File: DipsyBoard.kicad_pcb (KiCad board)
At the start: 2 copper layers, 30.5 x 45.7 mm, 28 parts, among them P2 CONN_01X16, P3 CONN_01X16, U1 STM32L486Rx-LQFP64, U2 LD1117S50TR, U4 PUSBMxX4, U5 TPS56x200, Y1 16MHz

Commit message: Last changes
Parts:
- removed C10, C11: 22pF, Capacitors_SMD:C_0603
- removed C15: 0.1u, Capacitors_SMD:C_0603
- removed C16: 22uF, Capacitors_SMD:C_1206
- removed L1: 3.3uH, SMD_Packages:SMD-1210_Pol
- removed R1: 33.2k, Resistors_SMD:R_0603
- removed R2: 10.0k, Resistors_SMD:R_0603
- removed U5: TPS56x200, Housings_SOT-23_SOT-143_TSOT-6:SOT-23-6
- removed Y1: 16MHz, Crystals:Crystal_SMD_0603_4Pads
- added C18: 0.1uF, w_smd_cap:c_0603, F.Cu at (151.2, 119.7)
- added CON1: SD_Card, xess:xess-SCHD3A0100, B.Cu at (144.7, 129.1)
- added P1: USB_OTG, w_conn_pc:conn_usb_B_mini_smd, F.Cu at (144.8, 100.3)
- added P6: JTAG, engstad:conn-jtag-0.05, B.Cu at (144.8, 101.7)
- added SW1: RESET, Buttons_Switches_SMD:SW_SPST_EVPBF, F.Cu at (145.0, 142.7)
- added U3: NCP1117DT33G, w_smd_trans:sot223, F.Cu at (149.6, 113.0)
- added X1: XTAL, engstad:cstce-v-c, F.Cu at (140.6, 119.5)
- C1, C5, C6, C7, C8, C9: footprint Capacitors_SMD:C_0603 -> w_smd_cap:c_0603
- C12, C13, C14, C2, C3, C4: footprint Capacitors_SMD:C_0805 -> w_smd_cap:c_0805
- C17: footprint Capacitors_SMD:C_1206 -> w_smd_cap:c_1206
- P2, P3: value CONN_01X16 -> CONN_01X19; footprint Pin_Headers:Pin_Header_Straight_1x16 -> w_pin_strip:pin_strip_19
- U2: value LD1117S50TR -> NCP1117ST50T3G; footprint Housings_SOT-23_SOT-143_TSOT-6:SOT-23 -> w_smd_trans:sot223
- moved C1 82.8 mm to (139.2, 142.7), turned to 90 degrees
- moved C7 76.9 mm to (150.2, 136.4), turned to 90 degrees
- moved C6 72.3 mm to (137.0, 122.4), turned to 270 degrees
- moved C2 63.1 mm to (140.8, 135.8)
- moved C9 62.6 mm to (140.5, 137.6)
- moved C8 50.3 mm to (149.5, 119.7), turned to 270 degrees
- moved C5 49.5 mm to (147.8, 119.7), turned to 270 degrees
- moved C3 47.2 mm to (137.2, 125.8), turned to 90 degrees
- moved C4 45.9 mm to (152.3, 134.9), turned to 90 degrees
- moved C13 44.5 mm to (152.0, 100.5), turned to 90 degrees
- moved C12 41.8 mm to (140.9, 107.3), turned to 180 degrees
- moved C14 36.1 mm to (149.9, 107.3), turned to 180 degrees
- moved D1 34.6 mm to (145.4, 107.3), turned to 180 degrees
- moved U4 31.2 mm to (145.1, 117.0)
- moved U2 30.2 mm to (139.9, 113.0), turned to 180 degrees
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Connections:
- net /OTG_FS_DM renamed /OTG_FS_D-
- net /OTG_FS_DP renamed /OTG_FS_D+
- C13 pad 1: Net-(C13-Pad1) -> /+5V
- D1 pad 2: Net-(C13-Pad1) -> /+5V
- P2 pad 1: /D1 -> /+5V
- P2 pad 11: /D11 -> /D9
- P2 pad 12: /D12 -> /D8
- P2 pad 13: /D13 -> /D7
- P2 pad 14: /D14 -> /D6
- P2 pad 15: /D15 -> /D5
- P2 pad 16: /D16 -> /D4
- P2 pad 2: /D2 -> GND
- P2 pad 3: /D3 -> /VDD
- P2 pad 4: /D4 -> /D16
- P2 pad 5: /D5 -> /D15
- P2 pad 6: /D6 -> /D14
- P2 pad 7: /D7 -> /D13
- P2 pad 8: /D8 -> /D12
- P2 pad 9: /D9 -> /D11
- P3 pad 1: /A1 -> /VIN
- P3 pad 10: /A10 -> /A7
- P3 pad 11: /A11 -> /A8
- P3 pad 12: /A12 -> /A9
- P3 pad 13: /A13 -> /A10
- P3 pad 14: /A14 -> /A11
- P3 pad 15: /A15 -> /A12
- P3 pad 16: /A16 -> /A13
- P3 pad 2: /A2 -> GND
- P3 pad 3: /A3 -> /RTC_OUT
- P3 pad 4: /A4 -> /A1
- P3 pad 5: /A5 -> /A2
- P3 pad 6: /A6 -> /A3
- P3 pad 7: /A7 -> /A4
- P3 pad 8: /A8 -> /A5
- P3 pad 9: /A9 -> /A6
- U1 pad 29: /D7 -> /D2
- U1 pad 30: /D8 -> /D3
- U1 pad 33: /D9 -> /D4
- U1 pad 34: /D10 -> /D5
- U1 pad 35: /D11 -> /D6
- U1 pad 36: /D12 -> /D7
- U1 pad 37: /D14 -> /D8
- U1 pad 38: /D15 -> /D9
- U1 pad 41: /OTG_FS_SOF -> /D10
- U1 pad 42: /OTG_FS_VBUS -> /D11
- U1 pad 57: /D2 -> /D12
- U1 pad 58: /D3 -> /D13
- U1 pad 59: /D4/PVD -> /D14
- U1 pad 61: /D5 -> /D15
- U1 pad 62: /D6 -> /D16
- U2 pad 2: Net-(C13-Pad1) -> /+5V
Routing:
- net /OTG_FS_D+: track 0.00 -> 38.3 mm, vias 0 -> 2
- net /OTG_FS_D-: track 0.00 -> 37.9 mm, vias 0 -> 2
- net /OTG_FS_ID: track 0.00 -> 37.4 mm
- net /JTMS: track 0.00 -> 32.7 mm, vias 0 -> 1
- net /+5V: track 0.00 -> 30.3 mm
- net /RTC_OUT: track 0.00 -> 28.8 mm, vias 0 -> 1
- net /VDD: track 0.00 -> 28.0 mm
- net /JTDI: track 0.00 -> 28.0 mm, vias 0 -> 1
- net /D16: track 0.00 -> 27.8 mm, vias 0 -> 1
- net GND: track 0.00 -> 26.5 mm
- net /JTCK: track 0.00 -> 26.4 mm, vias 0 -> 1
- net /JTDO: track 0.00 -> 25.2 mm, vias 0 -> 1
- net /D15: track 0.00 -> 24.8 mm, vias 0 -> 1
- net /~JTRST: track 0.00 -> 24.1 mm, vias 0 -> 1
- net /D14: track 0.00 -> 21.7 mm, vias 0 -> 1
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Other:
- board size 30.5 x 45.7 mm -> 22.9 x 50.8 mm
- net class Default: clearance 0.2 -> 0.2032; trace_width 0.25 -> 0.2032
- net class Power added: clearance 0.254, trace_width 0.381, via_dia 0.6, via_drill 0.4
- rule trace_clearance: 0.2 -> 0.2032

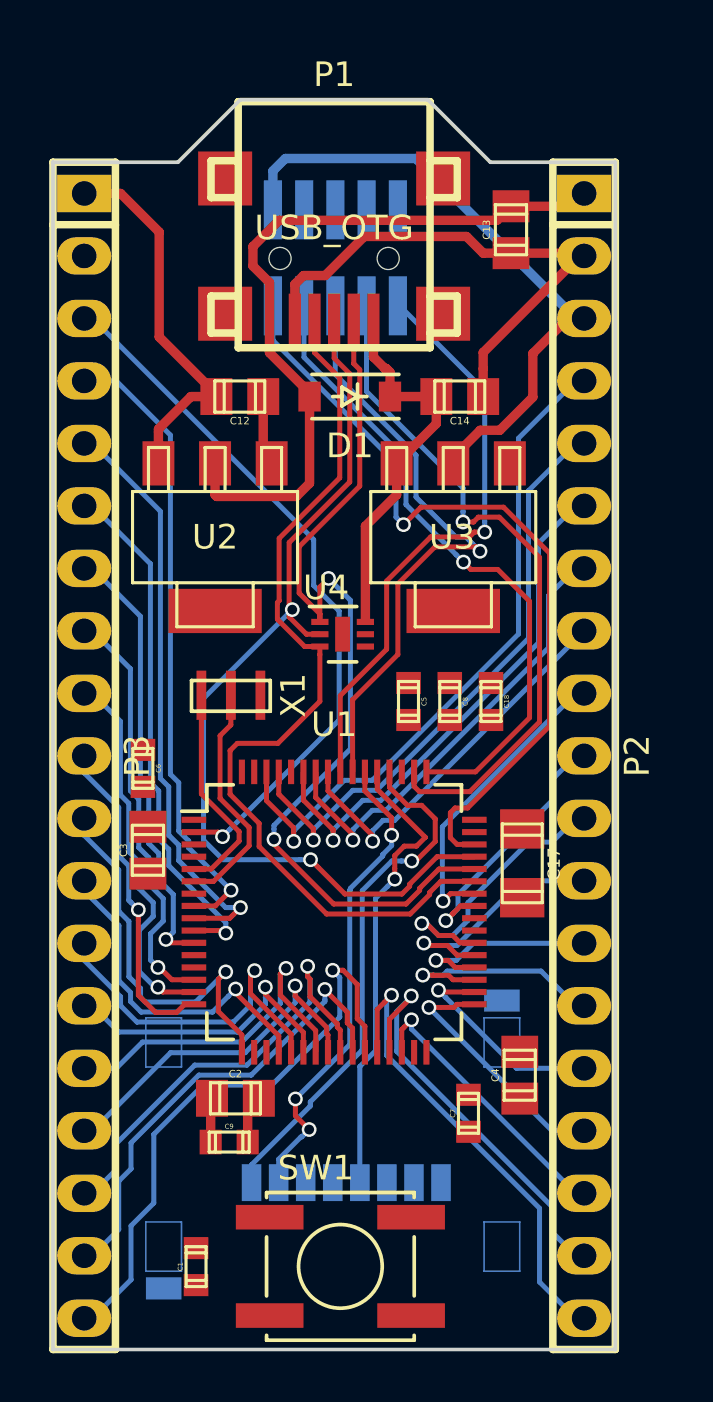
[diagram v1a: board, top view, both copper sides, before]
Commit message: Changes of power source
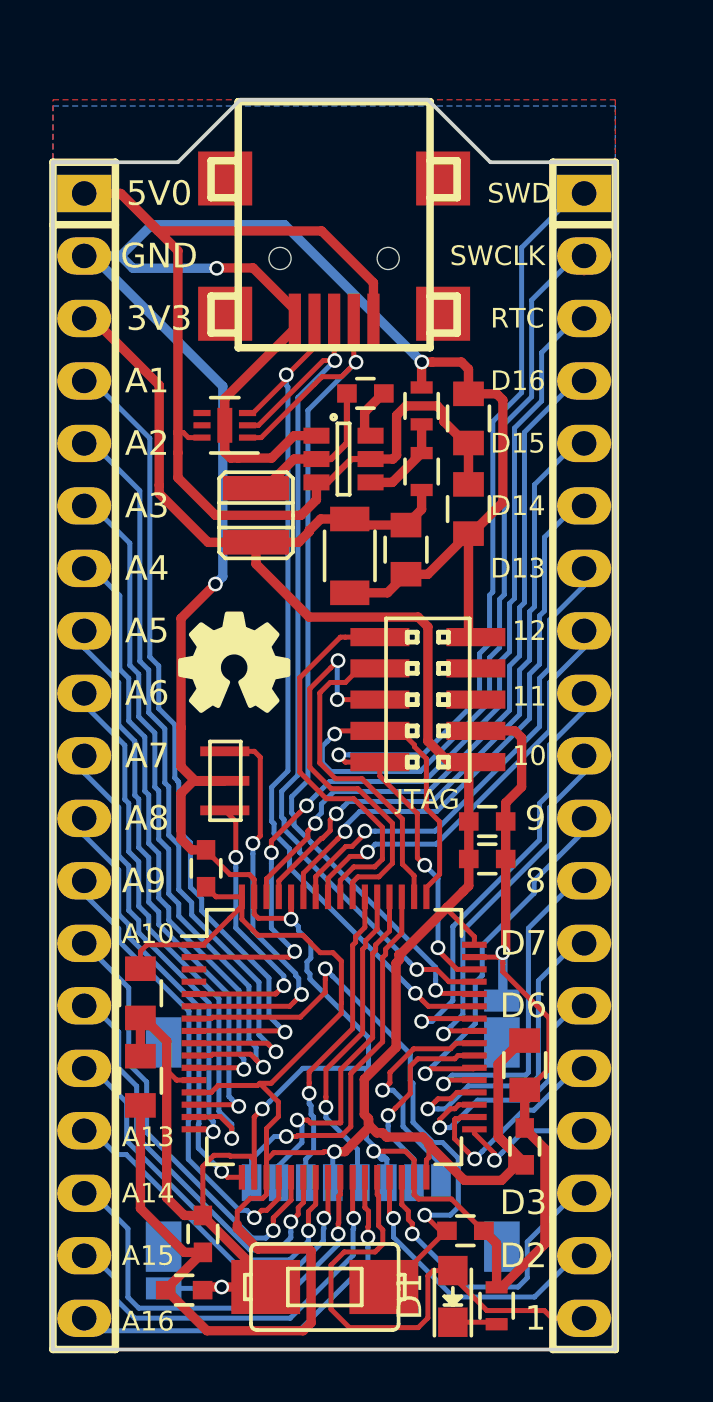
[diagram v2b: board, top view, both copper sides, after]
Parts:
- removed C12: 10uF(25V), w_smd_cap:c_0805
- removed C13: 10uF, w_smd_cap:c_0805
- removed C17: 22uF, w_smd_cap:c_1206
- removed U2: NCP1117ST50T3G, w_smd_trans:sot223
- added ?: , xess:oshw-logo2, F.Cu at (140.7, 118.1)
- added C10: 10uF, Capacitors_SMD:C_0805, F.Cu at (150.2, 108.2)
- added C11: 10uF, Capacitors_SMD:C_0805, F.Cu at (150.2, 111.9)
- added C15: 10uF, Capacitors_SMD:C_0805, F.Cu at (147.7, 113.5)
- added C16: 22uF, Capacitors_SMD:C_1206, F.Cu at (145.4, 113.8)
- added L1: 3.3uH, engstad:inductor-smd-1212, F.Cu at (141.6, 112.1)
- added R1: 33.2k, Resistors_SMD:R_0603, F.Cu at (148.3, 110.4)
- added R2: 10.0k, Resistors_SMD:R_0603, F.Cu at (148.3, 107.7)
- added R3: 470, Resistors_SMD:R_0603, F.Cu at (151.4, 144.3)
- C1, C18, C5, C6, C7, C8, C9: footprint w_smd_cap:c_0603 -> Capacitors_SMD:C_0603
- C14: value 10uF -> 0.1uF; footprint w_smd_cap:c_0805 -> Capacitors_SMD:C_0603
- C2, C3, C4: footprint w_smd_cap:c_0805 -> Capacitors_SMD:C_0805
- CON1: value SD_Card -> SDMMC_Card
- D1: value 2A/30V/0.375V -> RED; footprint Diodes_SMD:SOD-123 -> LEDs:LED-0805
- P6: moved to F.Cu
- SW1: value RESET -> SW_PUSH; footprint Buttons_Switches_SMD:SW_SPST_EVPBF -> engstad:tactile-switch-te-147873-2
- U3: value NCP1117DT33G -> TPS56x200; footprint w_smd_trans:sot223 -> Housings_SOT-23_SOT-143_TSOT-6:SOT-23-6
- moved D1 36.8 mm to (149.6, 143.9), turned to 90 degrees
- moved C18 27.0 mm to (138.7, 143.6), turned to 0 degrees
- moved P6 18.3 mm to (148.6, 119.6), turned to 90 degrees
- moved C6 14.5 mm to (151.0, 126.1), turned to 0 degrees
- moved C1 11.0 mm to (150.1, 141.2), turned to 0 degrees
- moved C5 10.7 mm to (139.6, 126.5), turned to 90 degrees
- moved U4 9.75 mm to (140.3, 108.5), turned to 180 degrees
- moved C3 5.82 mm to (136.9, 131.6), turned to 270 degrees
- moved U3 5.47 mm to (145.2, 109.9), turned to 0 degrees
- moved C8 5.11 mm to (151.0, 124.6), turned to 0 degrees
- moved U1 5.08 mm to (144.8, 133.3)
- moved C2 3.93 mm to (136.9, 135.1), turned to 90 degrees
- moved C9 3.88 mm to (139.4, 141.4), turned to 90 degrees
- moved C14 3.84 mm to (146.1, 107.2), turned to 0 degrees
- moved X1 3.49 mm to (140.3, 122.9), turned to 90 degrees
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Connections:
- C14 pad 1: /OTG_5V -> Net-(C14-Pad1)
- C14 pad 2: GND -> Net-(C14-Pad2)
- CON1 pad 1: /SDMMC_D3 -> /SDMMC_D2
- CON1 pad 2: /SDMMC_CMD -> /SDMMC_D3
- CON1 pad 3: GND -> /SDMMC_CMD
- CON1 pad G1: (no net) -> GND
- CON1 pad G2: (no net) -> GND
- D1 pad 1: /OTG_5V -> Net-(D1-Pad1)
- D1 pad 2: /+5V -> /D1
- P2 pad 1: /+5V -> /JTMS/SWDIO
- P2 pad 2: GND -> /JTCK/SWCLK
- P2 pad 3: /VDD -> /RTC_OUT
- P3 pad 1: /VIN -> /OTG_5V
- P3 pad 3: /RTC_OUT -> /VDD
- P6 pad 2: /JTMS -> /JTMS/SWDIO
- P6 pad 4: /JTCK -> /JTCK/SWCLK
- SW1 pad 1: /~RST -> GND
- SW1 pad 2: GND -> /~RST
- U1 pad 46: /JTMS -> /JTMS/SWDIO
- U1 pad 49: /JTCK -> /JTCK/SWCLK
- U3 pad 2: /VDD -> Net-(C14-Pad1)
- U3 pad 4: (no net) -> Net-(R1-Pad2)
- X1 pad 2: Net-(U1-Pad6) -> GND
- X1 pad 3: GND -> Net-(U1-Pad6)
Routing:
- net GND: track 26.5 -> 184.4 mm, vias 0 -> 8
- net /VDD: track 28.0 -> 136.3 mm, vias 0 -> 1
- net /JTMS/SWDIO: track 0.00 -> 41.7 mm, vias 0 -> 3
- net /JTCK/SWCLK: track 0.00 -> 40.5 mm, vias 0 -> 1
- net /JTMS: track 32.7 -> 0.00 mm, vias 1 -> 0
- net /OTG_5V: track 15.6 -> 46.6 mm
- net /+5V: track 30.3 -> 0.00 mm
- net /JTCK: track 26.4 -> 0.00 mm, vias 1 -> 0
- net /~RST: track 0.00 -> 25.1 mm, vias 0 -> 2
- net /SDMMC_D2: track 0.00 -> 15.7 mm, vias 0 -> 1
- net /VIN: track 15.6 -> 0.00 mm
- net /JTDI: track 28.0 -> 13.4 mm, vias 1 -> 0
- net /SDMMC_D1: track 0.00 -> 9.76 mm, vias 0 -> 1
- net /RTC_OUT: track 28.8 -> 38.0 mm, vias 1 -> 3
- net /JTDO: track 25.2 -> 16.7 mm, vias 1 -> 2
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- added copper zone on B.Cu, net GND
- added copper zone on F.Cu, net GND
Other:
- rule pad_to_mask_clearance: 0.2 -> 0
- rule trace_min: 0.2 -> 0.1524
- board text added: "1"
- board text added: "10"
- board text added: "11"
- board text added: "12"
- board text added: "3V3"
- board text added: "5V0"
- board text added: "8"
- board text added: "9"
- board text added: "A1"
- board text added: "A10"
- board text added: "A13"
- board text added: "A14"
- board text added: "A15"
- board text added: "A16"
- board text added: "A2"
- board text added: "A3"
- board text added: "A4"
- board text added: "A5"
- board text added: "A6"
- board text added: "A7"
- board text added: "A8"
- board text added: "A9"
- board text added: "BetsyBoard V0.1"
- board text added: "D13"
- board text added: "D14"
- board text added: "D15"
- board text added: "D16"
- board text added: "D2"
- board text added: "D3"
- board text added: "D6"
- board text added: "D7"
- board text added: "Engstad Design Studio"
- board text added: "GND"
- board text added: "No warranty! Use at your own risk."
- board text added: "RTC"
- board text added: "SWCLK"
- board text added: "SWD"

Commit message: v0.2
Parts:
- removed ?: , xess:oshw-logo2
- removed C14: 0.1uF, Capacitors_SMD:C_0603
- removed C15: 10uF, Capacitors_SMD:C_0805
- removed C16: 22uF, Capacitors_SMD:C_1206
- removed L1: 3.3uH, engstad:inductor-smd-1212
- removed R1: 33.2k, Resistors_SMD:R_0603
- removed R2: 10.0k, Resistors_SMD:R_0603
- added C12: 22uF, smd:SM1206, F.Cu at (113.6, 80.0)
- added C13: 22uF, smd:SM1206, F.Cu at (116.6, 80.0)
- added C17: 10pF, smd:SM0603, F.Cu at (126.3, 88.0)
- added C19: 10pF, smd:SM0603, F.Cu at (128.8, 88.0)
- added D2: DFLS240L, engstad:diode-smd-powerdi-123, F.Cu at (138.2, 63.2)
- added D3: GREEN, LEDs:LED-0805, F.Cu at (122.9, 60.6)
- added JP1: JUMPER3, xess:xess-JP2, F.Cu at (114.7, 75.1)
- added L2: 470nH, smd:SM0603, F.Cu at (120.6, 80.8)
- added L3: Bead, smd:SM0805, F.Cu at (136.7, 82.8)
- added P4: JLINK-SWD, xess:HDR_1x6, F.Cu at (111.0, 53.4)
- added P5: POWER, w_pin_strip:pin_socket_2, F.Cu at (144.0, 53.4)
- added R4: 10k, smd:SM0603, F.Cu at (120.7, 75.1)
- added R5: 470, smd:SM0603, F.Cu at (122.9, 63.8)
- added U2: NCP1117ST33T3G, TO_SOT_Packages_SMD:SOT-223, F.Cu at (137.2, 57.2)
- added Y1: Crystal, armory:CRYSTAL-32k-B, F.Cu at (127.5, 86.0)
- C1, C18, C5, C6, C7, C8, C9: footprint Capacitors_SMD:C_0603 -> smd:SM0603
- C10, C11, C2: footprint Capacitors_SMD:C_0805 -> smd:SM0805
- C3, C4: footprint Capacitors_SMD:C_0805 -> smd:SM0603
- CON1: footprint xess:xess-SCHD3A0100 -> engstad:SCHD3A0100; moved to F.Cu
- P1: footprint w_conn_pc:conn_usb_B_mini_smd -> engstad:usb-otg-short
- P2: value CONN_01X19 -> Analog; footprint w_pin_strip:pin_strip_19 -> Pin_Headers:Pin_Header_Straight_1x16
- P3: value CONN_01X19 -> Digital; footprint w_pin_strip:pin_strip_19 -> Pin_Headers:Pin_Header_Straight_1x16
- P6: value JTAG -> CORTEX-JTAG; footprint engstad:conn-jtag-0.05 -> engstad:smt-pin-header-02x05-127
- R3: footprint Resistors_SMD:R_0603 -> smd:SM0603
- U3: value TPS56x200 -> APX823; footprint Housings_SOT-23_SOT-143_TSOT-6:SOT-23-6 -> TO_SOT_Packages_SMD:SOT-23-5
- U4: value PUSBMxX4 -> PUSBM5V5X4; footprint Housings_DFN_QFN:DFN-6-1EP_2x2mm_Pitch0.5mm -> engstad:dfn1616-6
- moved D1 88.1 mm to (120.7, 60.6)
- moved R3 86.1 mm to (120.7, 63.8), turned to 270 degrees
- moved C18 74.9 mm to (136.9, 68.8)
- moved P3 71.3 mm to (104.7, 57.2), turned to 0 degrees
- moved C2 68.2 mm to (137.0, 66.9), turned to 0 degrees
- moved C7 67.7 mm to (121.2, 77.8)
- moved P6 66.7 mm to (113.9, 62.6)
- moved C8 63.7 mm to (123.8, 67.0), turned to 180 degrees
- moved C3 61.2 mm to (136.9, 70.4), turned to 0 degrees
- moved U1 60.7 mm to (128.9, 74.8), turned to 90 degrees
- moved C9 59.4 mm to (134.3, 82.2), turned to 180 degrees
- moved C4 54.0 mm to (134.3, 83.7), turned to 180 degrees
- moved C10 53.8 mm to (132.5, 57.4), turned to 270 degrees
- moved P1 53.7 mm to (125.1, 50.4)
- moved C11 53.3 mm to (132.5, 61.6), turned to 90 degrees
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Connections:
- net /JTDO renamed /JTDO/SWO
- C1 pad 1: /~RST -> VDD
- C11 pad 1: /OTG_5V -> VDD
- C18 pad 1: /VDD -> VDD
- C2 pad 1: /VDD -> VDD
- C3 pad 1: /VDD -> VDD
- C4 pad 1: /VDD -> +3.3VADC
- C5 pad 1: /VDD -> VDD
- C6 pad 1: /VDD -> VDD
- C7 pad 1: /VDD -> VDD
- C8 pad 1: /VDD -> VDD
- C9 pad 1: /VDD -> +3.3VADC
- CON1 pad 4: /VDD -> Net-(C12-Pad1)
- P2 pad 1: /JTMS/SWDIO -> /A1
- P2 pad 10: /D10 -> /A10
- P2 pad 11: /D9 -> /A11
- P2 pad 12: /D8 -> /A12
- P2 pad 13: /D7 -> /A13
- P2 pad 14: /D6 -> /A14
- P2 pad 15: /D5 -> /A15
- P2 pad 16: /D4 -> /A16
- P2 pad 2: /JTCK/SWCLK -> /A2
- P2 pad 3: /RTC_OUT -> /A3
- P2 pad 4: /D16 -> /A4
- P2 pad 5: /D15 -> /A5
- P2 pad 6: /D14 -> /A6
- P2 pad 7: /D13 -> /A7
- P2 pad 8: /D12 -> /A8
- P2 pad 9: /D11 -> /A9
- P3 pad 1: /OTG_5V -> /D1
- P3 pad 10: /A7 -> /D10
- P3 pad 11: /A8 -> /D11
- P3 pad 12: /A9 -> /D12
- P3 pad 13: /A10 -> /D13
- P3 pad 14: /A11 -> /D14
- P3 pad 15: /A12 -> /D15
- P3 pad 16: /A13 -> /D16
- P3 pad 2: GND -> /D2
- P3 pad 3: /VDD -> /D3
- P3 pad 4: /A1 -> /D4
- P3 pad 5: /A2 -> /D5
- P3 pad 6: /A3 -> /D6
- P3 pad 7: /A4 -> /D7
- P3 pad 8: /A5 -> /D8
- P3 pad 9: /A6 -> /D9
- P6 pad 1: /VDD -> VDD
- P6 pad 10: /~JTRST -> /~RST
- P6 pad 7: GND -> Net-(P6-Pad7)
- SW1 pad 2: /~RST -> Net-(SW1-Pad2)
- U1 pad 1: /VDD -> VDD
- U1 pad 13: /VDD -> +3.3VADC
- U1 pad 19: /VDD -> VDD
- U1 pad 2: /RTC_OUT -> /RTC
- U1 pad 3: Net-(U1-Pad3) -> /RTC_OSC_IN
- U1 pad 32: /VDD -> VDD
- U1 pad 4: Net-(U1-Pad4) -> /RTC_OSC_OUT
- U1 pad 48: /VDD -> VDD
- U1 pad 56: /~JTRST -> /~RST
- U1 pad 60: GND -> /BOOT0
- U1 pad 64: /VDD -> VDD
- U3 pad 1: GND -> /~RST
- U3 pad 2: Net-(C14-Pad1) -> GND
- U3 pad 3: /OTG_5V -> Net-(SW1-Pad2)
- U3 pad 5: /OTG_5V -> VDD
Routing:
- net VDD: track 0.00 -> 159.7 mm
- net GND: track 184.4 -> 324.1 mm, vias 8 -> 17
- net /VDD: track 136.3 -> 0.00 mm, vias 1 -> 0
- net /~RST: track 25.1 -> 64.5 mm, vias 2 -> 4
- net /RTC_OUT: track 38.0 -> 0.00 mm, vias 3 -> 0
- net /D1: track 20.6 -> 53.1 mm, vias 0 -> 2
- net /D4: track 5.74 -> 37.3 mm
- net /SDMMC_D0: track 8.32 -> 38.3 mm, vias 1 -> 2
- net /D2: track 12.0 -> 41.5 mm
- net /SDMMC_D1: track 9.76 -> 39.2 mm, vias 1 -> 2
- net /JTDO/SWO: track 16.7 -> 45.7 mm, vias 2 -> 1
- net /D3: track 12.8 -> 41.4 mm
- net /D5: track 8.76 -> 35.9 mm
- net /SDMMC_D2: track 15.7 -> 40.0 mm, vias 1 -> 0
- net /SDMMC_D3: track 14.8 -> 38.2 mm, vias 1 -> 0
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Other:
- board size 22.9 x 50.8 mm -> 50 x 50 mm
- net class Default: clearance 0.2032 -> 0.2; trace_width 0.2032 -> 0.25
- net class Power removed
- rule trace_clearance: 0.2032 -> 0.2
- rule trace_min: 0.1524 -> 0.127
- board text added: "5.0V"
- board text added: "A11"
- board text added: "A12"
- board text added: "D1"
- board text added: "D10"
- board text added: "D11"
- board text added: "D4"
- board text added: "D5"
- board text added: "D8"
- board text added: "D9"
- board text added: "FLASH BOOT"
- board text added: "PA0"
- board text added: "PA1"
- board text added: "PA2"
- board text added: "PA3"
- board text added: "PA4"
- board text added: "PA5"
- board text added: "PA6"
- board text added: "PA7"
- board text added: "PA8"
- board text added: "PA9"
- board text added: "PB0"
- board text added: "PB1"
- board text added: "PB10"
- board text added: "PB11"
- board text added: "PB12"
- board text added: "PB13"
- board text added: "PB14"
- board text added: "PB15"
- board text added: "PB2"
- board text added: "PB5"
- board text added: "PB6"
- board text added: "PB7"
- board text added: "PB8"
- board text added: "PB9"
- board text added: "PC0"
- board text added: "PC1"
- board text added: "PC2"
- board text added: "PC3"
- board text added: "PC4"
- board text added: "PC5"
- board text added: "PC6"
- board text added: "PC7"
- board text removed: "1"
- board text removed: "10"
- board text removed: "11"
- board text removed: "12"
- board text removed: "3V3"
- board text removed: "5V0"
- board text removed: "8"
- board text removed: "9"
- board text removed: "BetsyBoard V0.1"
- board text removed: "D13"
- board text removed: "D14"
- board text removed: "D15"
- board text removed: "D16"
- board text removed: "No warranty! Use at your own risk."
- board text removed: "RTC"
- board text removed: "SWCLK"
- board text removed: "SWD"

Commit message: More work
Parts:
- removed D2: DFLS240L, engstad:diode-smd-powerdi-123
- added C14: 1nF, smd:SM0603, F.Cu at (139.9, 59.7)
- added C16: 10uF, smd:SM0805, F.Cu at (134.3, 61.7)
- added L1: 1.5uH, engstad:inductor-smd-1212, F.Cu at (135.3, 56.8)
- added R1: 560k, smd:SM0603, F.Cu at (137.6, 61.0)
- added R2: 180k, smd:SM0603, F.Cu at (137.6, 59.6)
- added R6: 1M, smd:SM0603, F.Cu at (137.6, 62.6)
- U2: value NCP1117ST33T3G -> TPS63051; footprint TO_SOT_Packages_SMD:SOT-223 -> engstad:dsbga-12
- moved U2 1.01 mm to (138.2, 57.4)
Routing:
- net GND: track 324.1 -> 338.3 mm, vias 17 -> 19
- net /PG: track 0.00 -> 8.48 mm
- net VDD: track 159.7 -> 163.1 mm
- net Net-(L1-Pad1): track 0.00 -> 3.35 mm
- net Net-(R1-Pad2): track 0.00 -> 3.11 mm
- net Net-(L1-Pad2): track 0.00 -> 2.72 mm
- net Net-(C14-Pad1): track 0.00 -> 1.66 mm
- net /OTG_5V: track 35.8 -> 34.5 mm
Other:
- rule pad_to_mask_clearance: 0 -> 0.05
